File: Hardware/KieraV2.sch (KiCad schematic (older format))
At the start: 21 parts, among them J1 Conn_01x06_Male, J2 Conn_01x04_Male, SW1 SW_Rotary2x4, SW2 SW_Rotary2x4, SW3 SW_Push, SW4 SW_Push, SW5 SW_Push, U1 STM32L4P5RET6

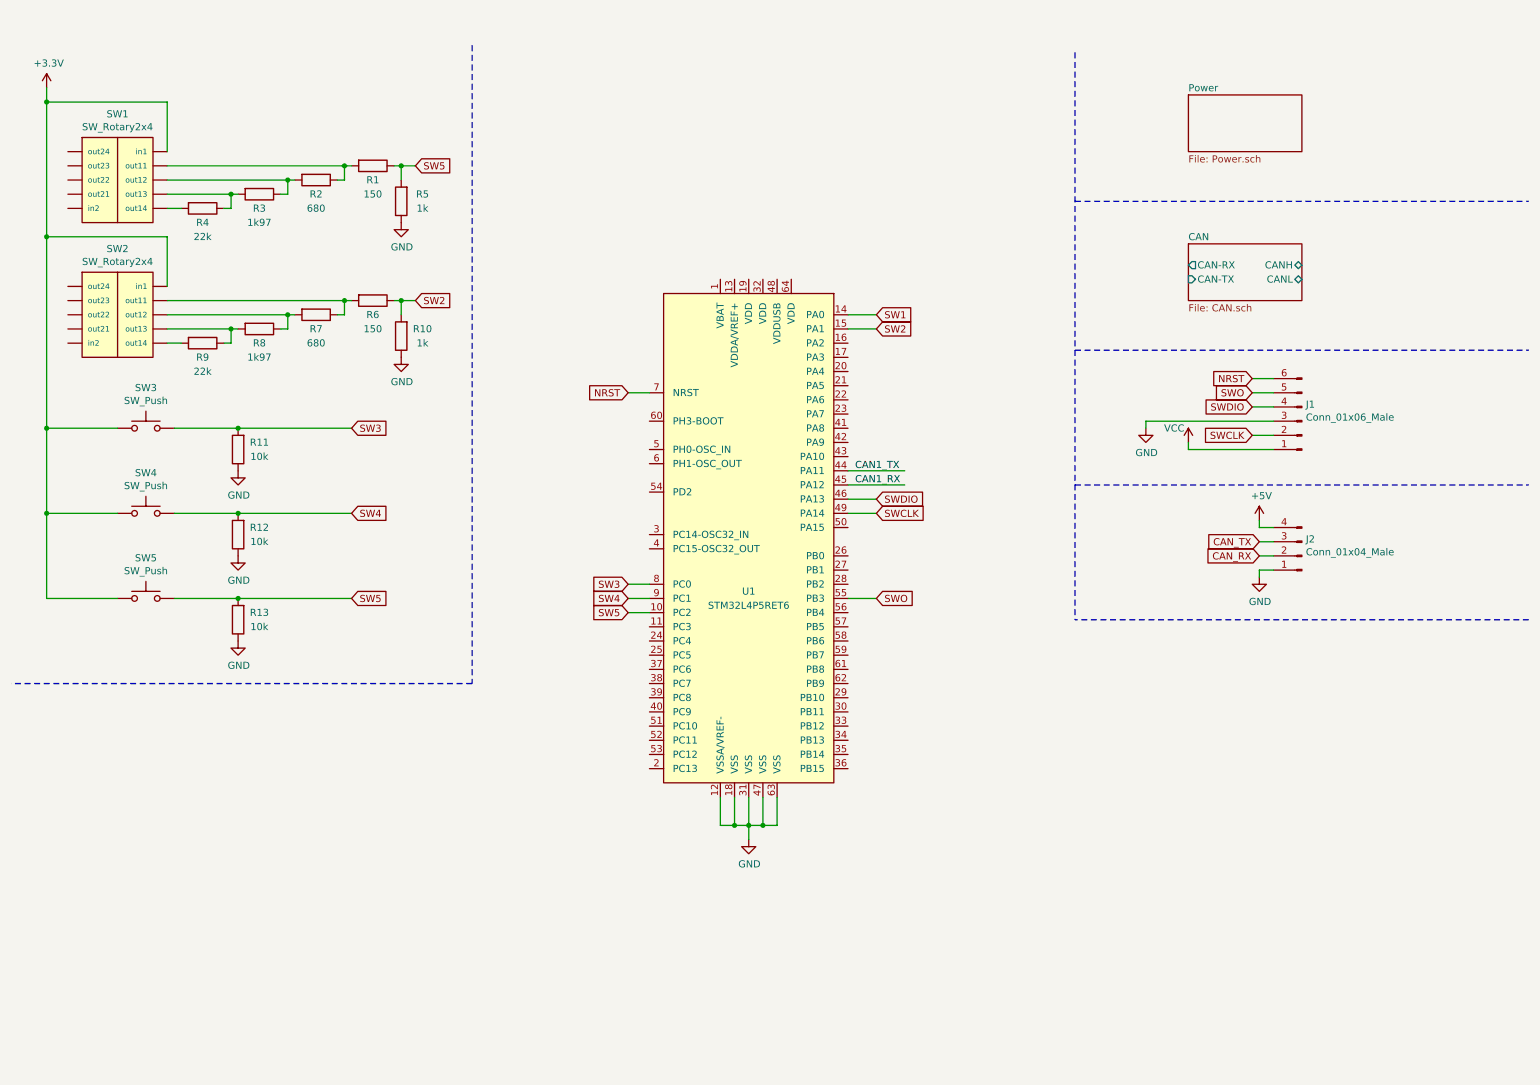
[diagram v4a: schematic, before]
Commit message: finished power scheme and some cosmetics
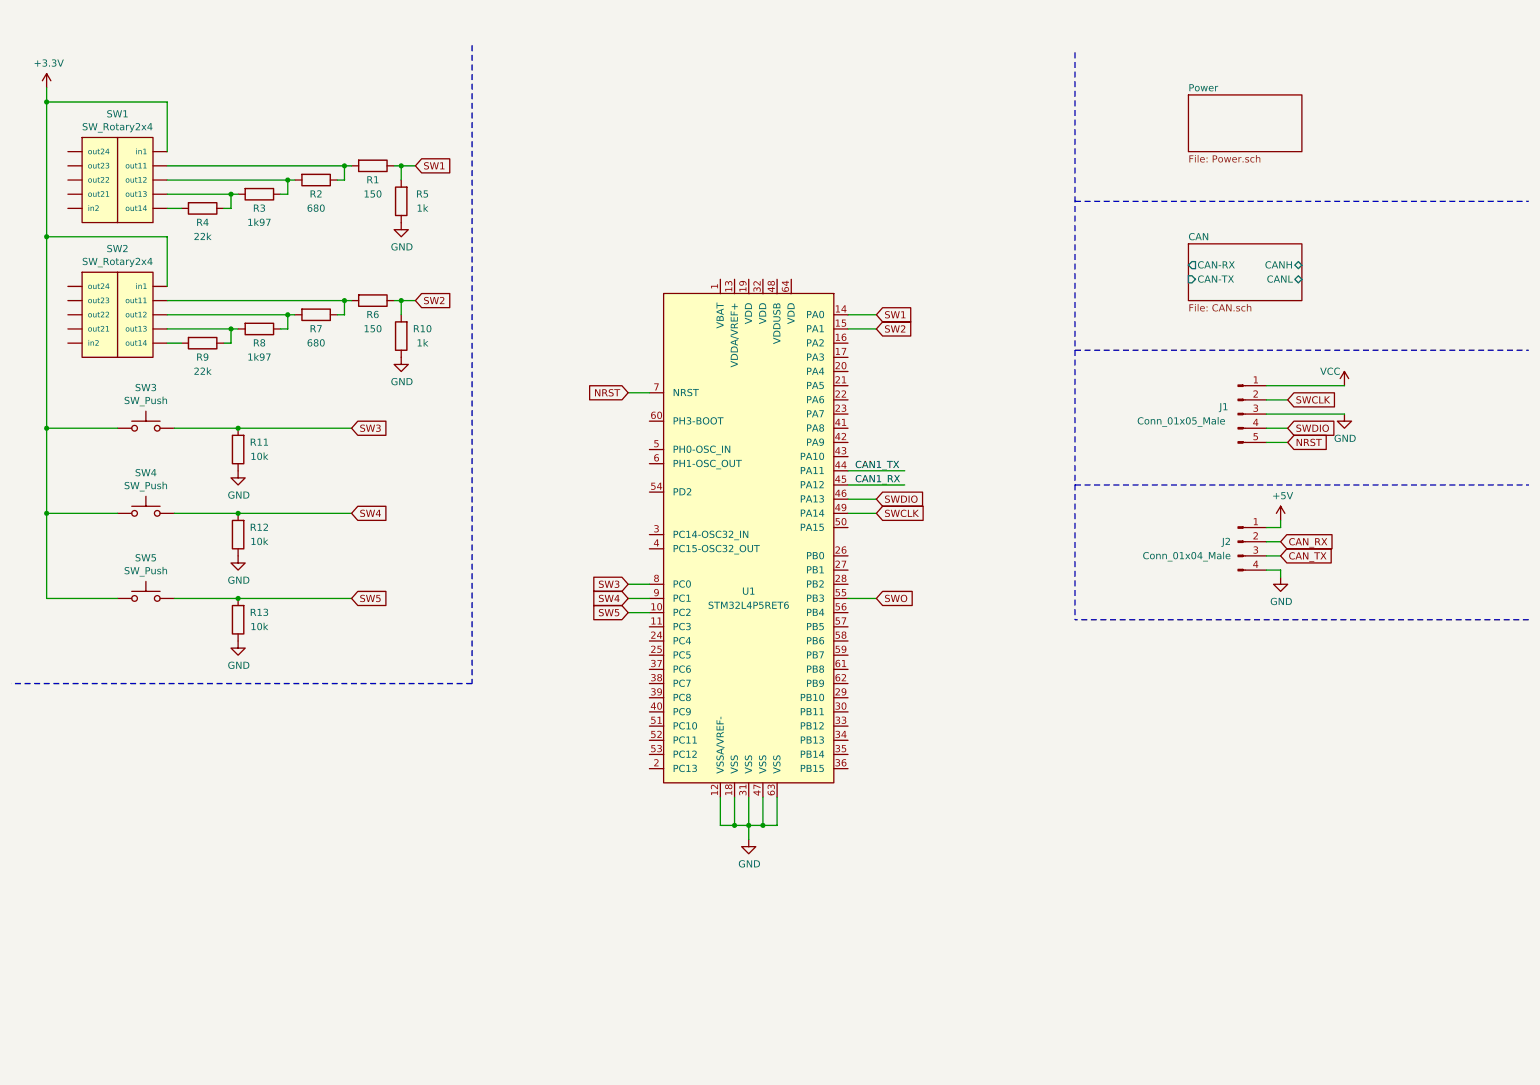
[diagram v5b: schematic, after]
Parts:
- removed J1: Conn_01x06_Male, symbol Connector:Conn_01x06_Male
- added J1: Conn_01x05_Male, symbol Connector:Conn_01x05_Male
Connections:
- net +5V: now also J2.1 (Pin_1); no longer J2.4 (Pin_4)
- net GND: now also J2.4 (Pin_4), J1.3 (Pin_3); no longer J2.1 (Pin_1)
- net NRST: now also J1.5 (Pin_5)
- net SW1: now also R1.1, R5.2
- net SW5: no longer R1.1, R5.2
- net SWCLK: now also J1.2 (Pin_2)
- net SWDIO: now also J1.4 (Pin_4)
- net VCC: now also J1.1 (Pin_1)
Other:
- moved on the sheet: J2
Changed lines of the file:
@@
 SW2
 Text GLabel 3350 1350 2    50   Input ~ 0
-SW5
+SW1
 Connection ~ 2100 3800
 $Sheet
@@
 Wire Notes Line
 	3750 5000 500  5000
-$Comp
-L Connector:Conn_01x06_Male J1
-U 1 1 61A68069
-P 9600 3150
-F 0 "J1" H 9572 3032 50  0000 R CNN
-F 1 "Conn_01x06_Male" H 9572 3123 50  0000 R CNN
-F 2 "" H 9600 3150 50  0001 C CNN
-F 3 "~" H 9600 3150 50  0001 C CNN
-	1    9600 3150
-	-1   0    0    1
-$EndComp
 Wire Wire Line
 	4850 2950 5000 2950
@@
 Text GLabel 6600 4400 2    50   Input ~ 0
 SWO
-Text GLabel 9250 2950 0    50   Input ~ 0
-SWO
-Text GLabel 9250 3050 0    50   Input ~ 0
+Text GLabel 9500 3200 2    50   Input ~ 0
 SWDIO
-Text GLabel 9250 2850 0    50   Input ~ 0
+Text GLabel 9500 3300 2    50   Input ~ 0
 NRST
 $Comp
 L power:GND #PWR?
 U 1 1 61A4CEAD
-P 8500 3200
-F 0 "#PWR?" H 8500 2950 50  0001 C CNN
-F 1 "GND" H 8505 3027 50  0000 C CNN
-F 2 "" H 8500 3200 50  0001 C CNN
-F 3 "" H 8500 3200 50  0001 C CNN
-	1    8500 3200
-	1    0    0    -1
-$EndComp
-Text GLabel 9250 3250 0    50   Input ~ 0
+P 9900 3100
+F 0 "#PWR?" H 9900 2850 50  0001 C CNN
+F 1 "GND" H 9905 2927 50  0000 C CNN
+F 2 "" H 9900 3100 50  0001 C CNN
+F 3 "" H 9900 3100 50  0001 C CNN
+	1    9900 3100
+	1    0    0    -1
+$EndComp
+Text GLabel 9500 3000 2    50   Input ~ 0
 SWCLK
 $Comp
 L power:VCC #PWR?
 U 1 1 61A51913
-P 8800 3300
-F 0 "#PWR?" H 8800 3150 50  0001 C CNN
-F 1 "VCC" H 8700 3400 50  0000 C CNN
-F 2 "" H 8800 3300 50  0001 C CNN
-F 3 "" H 8800 3300 50  0001 C CNN
-	1    8800 3300
-	1    0    0    -1
-$EndComp
-Wire Wire Line
-	8500 3200 8500 3150
-Wire Wire Line
-	8500 3150 9400 3150
-Wire Wire Line
-	8800 3300 8800 3350
-Wire Wire Line
-	8800 3350 9400 3350
-Wire Wire Line
-	9400 3250 9250 3250
-Wire Wire Line
-	9250 3050 9400 3050
-Wire Wire Line
-	9400 2950 9250 2950
-Wire Wire Line
-	9250 2850 9400 2850
+P 9900 2900
+F 0 "#PWR?" H 9900 2750 50  0001 C CNN
+F 1 "VCC" H 9800 3000 50  0000 C CNN
+F 2 "" H 9900 2900 50  0001 C CNN
+F 3 "" H 9900 2900 50  0001 C CNN
+	1    9900 2900
+	1    0    0    -1
+$EndComp
+Wire Wire Line
+	9350 3000 9500 3000
+Wire Wire Line
+	9500 3200 9350 3200
+Wire Wire Line
+	9350 3300 9500 3300
 Wire Notes Line
 	8000 2650 11200 2650
@@
 L Connector:Conn_01x04_Male J2
 U 1 1 61A93711
-P 9600 4100
-F 0 "J2" H 9572 3982 50  0000 R CNN
-F 1 "Conn_01x04_Male" H 9572 4073 50  0000 R CNN
-F 2 "" H 9600 4100 50  0001 C CNN
-F 3 "~" H 9600 4100 50  0001 C CNN
-	1    9600 4100
-	-1   0    0    1
-$EndComp
-Wire Wire Line
-	9400 3900 9300 3900
-Wire Wire Line
-	9300 3900 9300 3850
-Wire Wire Line
-	9400 4200 9300 4200
-Wire Wire Line
-	9300 4200 9300 4250
-Wire Wire Line
-	9400 4100 9300 4100
-Wire Wire Line
-	9400 4000 9300 4000
-Text GLabel 9300 4000 0    50   Input ~ 0
+P 9150 4000
+F 0 "J2" H 9100 4000 50  0000 R CNN
+F 1 "Conn_01x04_Male" H 9100 3900 50  0000 R CNN
+F 2 "" H 9150 4000 50  0001 C CNN
+F 3 "~" H 9150 4000 50  0001 C CNN
+	1    9150 4000
+	1    0    0    -1
+$EndComp
+Wire Wire Line
+	9350 4200 9450 4200
+Wire Wire Line
+	9450 4200 9450 4250
+Wire Wire Line
+	9350 3900 9450 3900
+Wire Wire Line
+	9450 3900 9450 3850
+Wire Wire Line
+	9350 4000 9450 4000
+Wire Wire Line
+	9350 4100 9450 4100
+Text GLabel 9450 4100 2    50   Input ~ 0
 CAN_TX
-Text GLabel 9300 4100 0    50   Input ~ 0
+Text GLabel 9450 4000 2    50   Input ~ 0
 CAN_RX
 $Comp
 L power:+5V #PWR?
 U 1 1 61A9DC54
-P 9300 3850
-F 0 "#PWR?" H 9300 3700 50  0001 C CNN
-F 1 "+5V" H 9315 4023 50  0000 C CNN
-F 2 "" H 9300 3850 50  0001 C CNN
-F 3 "" H 9300 3850 50  0001 C CNN
-	1    9300 3850
+P 9450 3850
+F 0 "#PWR?" H 9450 3700 50  0001 C CNN
+F 1 "+5V" H 9465 4023 50  0000 C CNN
+F 2 "" H 9450 3850 50  0001 C CNN
+F 3 "" H 9450 3850 50  0001 C CNN
+	1    9450 3850
 	1    0    0    -1
 $EndComp
@@
 L power:GND #PWR?
 U 1 1 61A9F0B3
-P 9300 4250
-F 0 "#PWR?" H 9300 4000 50  0001 C CNN
-F 1 "GND" H 9305 4077 50  0000 C CNN
-F 2 "" H 9300 4250 50  0001 C CNN
-F 3 "" H 9300 4250 50  0001 C CNN
-	1    9300 4250
+P 9450 4250
+F 0 "#PWR?" H 9450 4000 50  0001 C CNN
+F 1 "GND" H 9455 4077 50  0000 C CNN
+F 2 "" H 9450 4250 50  0001 C CNN
+F 3 "" H 9450 4250 50  0001 C CNN
+	1    9450 4250
 	1    0    0    -1
 $EndComp
@@
 F1 "Power.sch" 50
 $EndSheet
+$Comp
+L Connector:Conn_01x05_Male J1
+U 1 1 61ACE4C5
+P 9150 3100
+F 0 "J1" H 9050 3150 50  0000 C CNN
+F 1 "Conn_01x05_Male" H 8750 3050 50  0000 C CNN
+F 2 "" H 9150 3100 50  0001 C CNN
+F 3 "~" H 9150 3100 50  0001 C CNN
+	1    9150 3100
+	1    0    0    -1
+$EndComp
+Wire Wire Line
+	9900 3100 9350 3100
+Wire Wire Line
+	9900 2900 9350 2900
 $EndSCHEMATC

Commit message: uC supply added
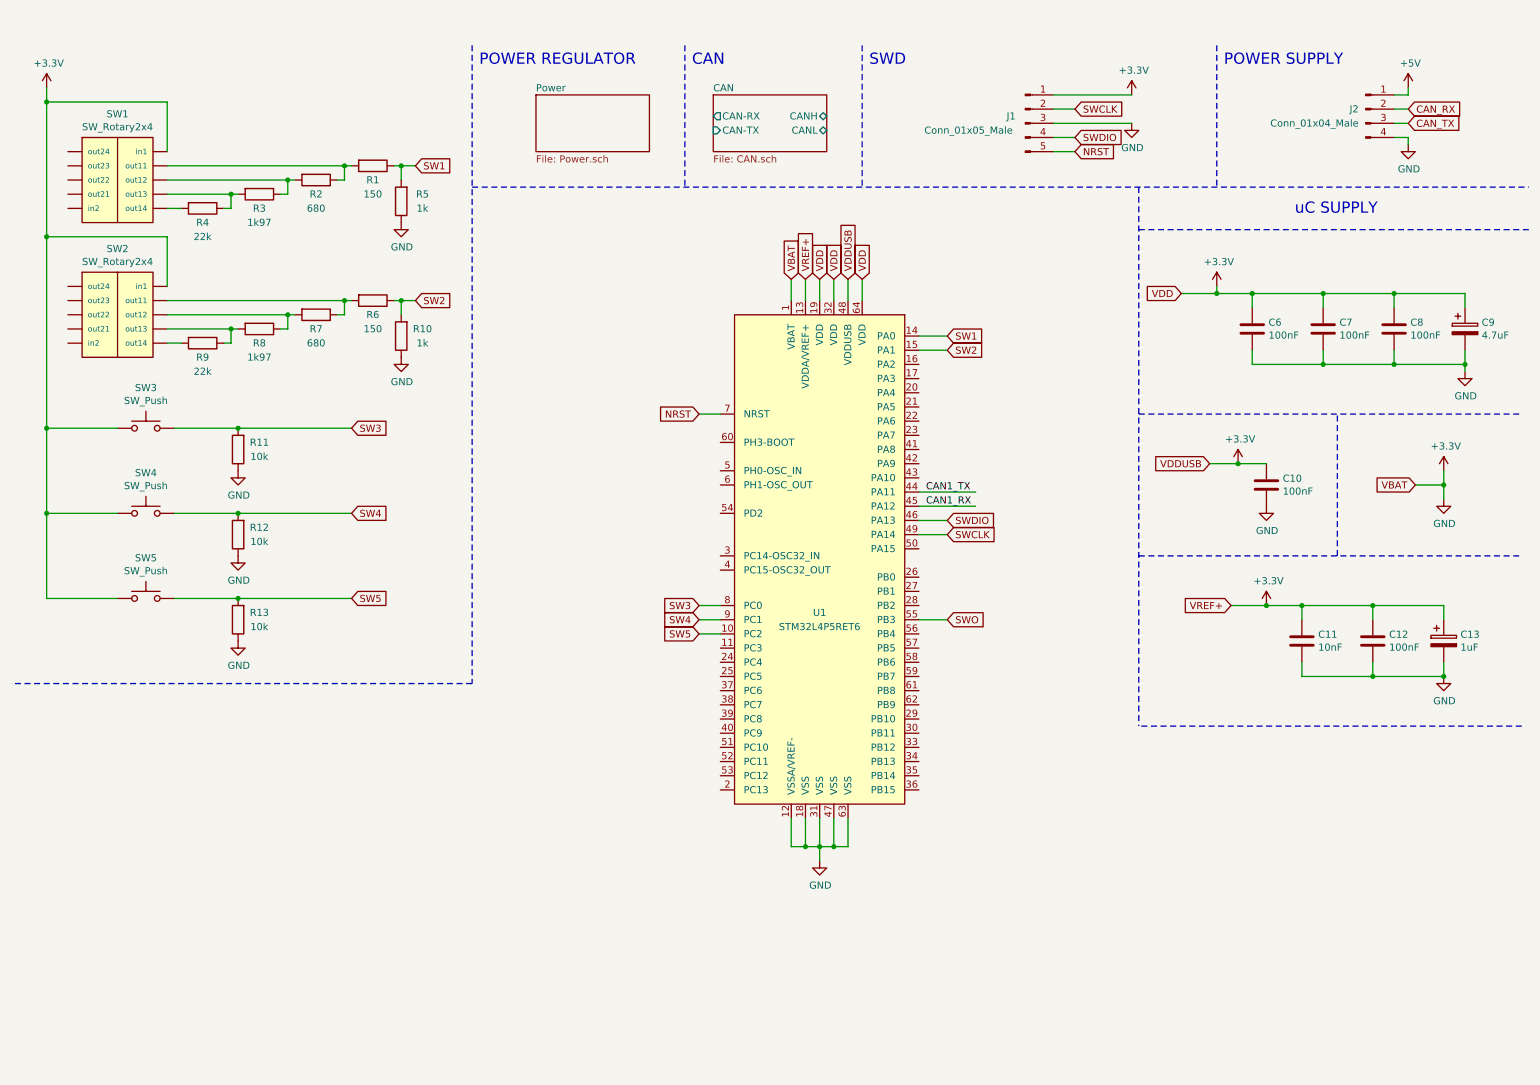
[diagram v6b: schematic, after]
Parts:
- added C10, C12, C6, C7, C8: 100nF, symbol Device:C
- added C11: 10nF, symbol Device:C
- added C13: 1uF, symbol Device:CP
- added C9: 4.7uF, symbol Device:CP
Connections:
- net GND is gone; now on net +3V3: J1.3 (Pin_3), J2.4 (Pin_4), R10.1, R11.1, R12.1, R13.1, R5.1, U1.12 (VSSA/VREF-), U1.18 (VSS), U1.31 (VSS), U1.47 (VSS), U1.63 (VSS)
- net VCC is gone; now on net +3V3: J1.1 (Pin_1)
- net +3V3: now also U1.1 (VBAT), U1.13 (VDDA/VREF+), U1.19 (VDD), U1.32 (VDD), U1.48 (VDDUSB), U1.64 (VDD), C10.1, C10.2, C11.1, C11.2, C12.1, C12.2, C13.1, C13.2, C6.1, C6.2, C7.1, C7.2, C8.1, C8.2, C9.1, C9.2
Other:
- note added: "CAN"
- note added: "POWER REGULATOR"
- note added: "POWER SUPPLY"
- note added: "SWD"
- note added: "uC SUPPLY"
- moved on the sheet: J1, J2, U1

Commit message: added reset button
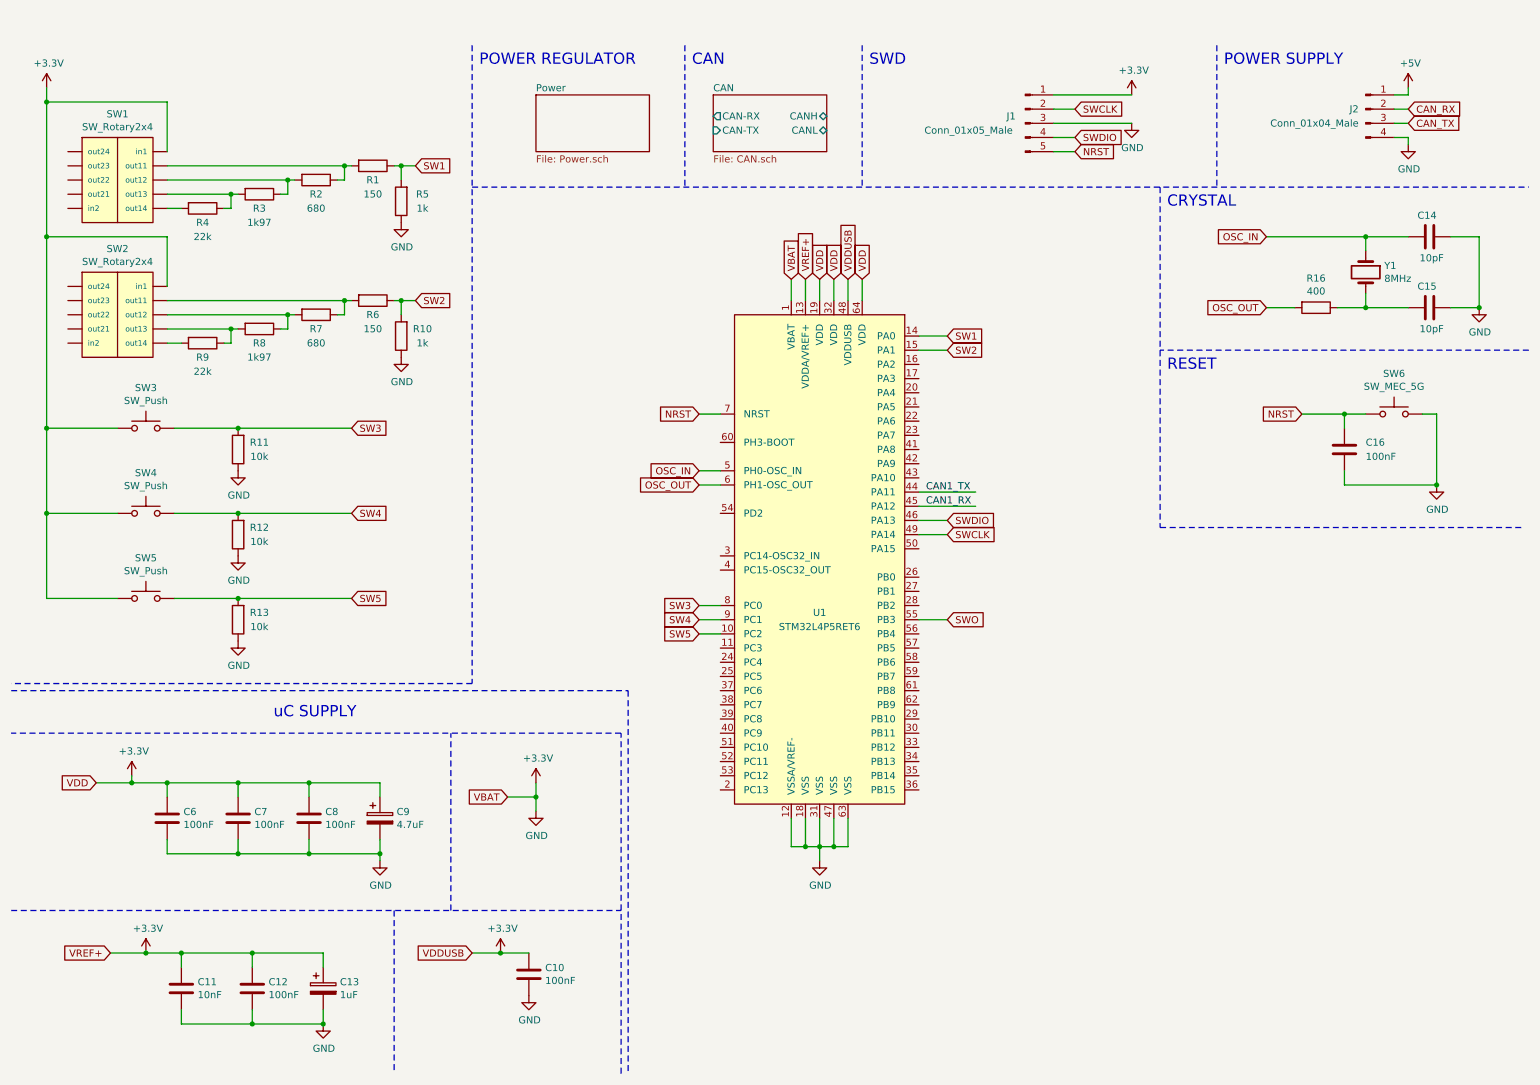
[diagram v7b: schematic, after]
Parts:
- added C14, C15: 10pF, symbol Device:C
- added C16: 100nF, symbol Device:C
- added R16: 400, symbol Device:R
- added SW6: SW_MEC_5G, symbol Switch:SW_MEC_5G
- added Y1: 8MHz, symbol Device:Crystal
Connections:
- net +3V3: now also C14.2, C15.2, C16.2, SW6.3 (B), SW6.4 (B)
- net NRST: now also C16.1, SW6.1 (A), SW6.2 (A)
- net OSC_IN: now reaches U1.5 (PH0-OSC_IN)
- net OSC_IN: now also C14.1, Y1.1
- net OSC_OUT: now reaches U1.6 (PH1-OSC_OUT)
- net OSC_OUT: now also R16.2
- new net: C15.1, R16.1, Y1.2
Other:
- note added: "CRYSTAL"
- note added: "RESET"
- moved on the sheet: C10, C11, C12, C13, C6, C7, C8, C9

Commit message: ready to review
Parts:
- added C17: 100nF, symbol Device:C
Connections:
- net +3V3: now also C17.1; no longer C10.2, C11.2, C12.2, C13.2, C14.2, C15.2, C16.2, C6.2, C7.2, C8.2, C9.2, J1.3 (Pin_3), J2.4 (Pin_4), R10.1, R11.1, R12.1, R13.1, R5.1, SW6.3 (B), SW6.4 (B), U1.12 (VSSA/VREF-), U1.18 (VSS), U1.31 (VSS), U1.47 (VSS), U1.63 (VSS)
- new net GND: C10.2, C11.2, C12.2, C13.2, C14.2, C15.2, C16.2, C17.2, C6.2, C7.2, C8.2, C9.2, J1.3 (Pin_3), J2.4 (Pin_4), R10.1, R11.1, R12.1, R13.1, R5.1, SW6.3 (B), SW6.4 (B), U1.12 (VSSA/VREF-), U1.18 (VSS), U1.31 (VSS), U1.47 (VSS), U1.63 (VSS)
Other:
- note added: "SWITCHES"
- moved on the sheet: C10, C11, C12, C13, C6, C7, C8, C9
